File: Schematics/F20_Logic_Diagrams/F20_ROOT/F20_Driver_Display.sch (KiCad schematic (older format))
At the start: 2 parts, among them U5 StepDownConverter, U6 Driver_Display

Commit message: Updated Brakes diagram. Updated power management diagram. Updated relevant library symbols. Updated README.
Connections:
- net labels added: DD_PWR
- net labels removed: PWR_AUX
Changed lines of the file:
@@
 $Descr A 11000 8500
 encoding utf-8
-Sheet 5 6
+Sheet 4 7
 Title "FSAE"
 Date "2020-01-22"
@@
 	2000 3250 2500 3250
 Text GLabel 2000 3000 0    50   Input ~ 0
-PWR_AUX
+DD_PWR
 Wire Wire Line
 	2000 3000 2500 3000

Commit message: Added GND and GND_CHASSIS symbols, updated relevant schematics. Restructured Powertrain hierarchy. Created ECU Connector symbols.
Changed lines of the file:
@@
 $Descr A 11000 8500
 encoding utf-8
-Sheet 4 7
+Sheet 3 7
 Title "FSAE"
-Date "2020-01-22"
-Rev "A"
+Date "2020-02-03"
+Rev "B"
 Comp "F20"
 Comment1 "Alex Domagala"
@@
 	1    0    0    -1
 $EndComp
-$Comp
-L power:GND #PWR?
-U 1 1 5E2A2C36
-P 3500 3500
-F 0 "#PWR?" H 3500 3250 50  0001 C CNN
-F 1 "GND" H 3505 3327 50  0000 C CNN
-F 2 "" H 3500 3500 50  0001 C CNN
-F 3 "" H 3500 3500 50  0001 C CNN
-	1    3500 3500
-	1    0    0    -1
-$EndComp
 Text GLabel 5000 3500 0    50   Input ~ 0
 RIM_DD_RX
@@
 Wire Wire Line
 	5000 4000 8000 4000
-$Comp
-L power:GND #PWR?
-U 1 1 5E29034E
-P 2000 3500
-F 0 "#PWR?" H 2000 3250 50  0001 C CNN
-F 1 "GND" H 2005 3327 50  0000 C CNN
-F 2 "" H 2000 3500 50  0001 C CNN
-F 3 "" H 2000 3500 50  0001 C CNN
-	1    2000 3500
-	1    0    0    -1
-$EndComp
 Wire Wire Line
 	2000 3500 2000 3250
@@
 Wire Wire Line
 	2000 3000 2500 3000
+$Comp
+L FSAE_Library:GND #PWR?
+U 1 1 5E3C0D7F
+P 2000 3500
+F 0 "#PWR?" H 2000 3300 50  0001 C CNN
+F 1 "GND" H 2004 3346 50  0000 C CNN
+F 2 "" H 2000 3450 50  0001 C CNN
+F 3 "" H 2000 3450 50  0001 C CNN
+	1    2000 3500
+	1    0    0    -1
+$EndComp
+$Comp
+L FSAE_Library:GND #PWR?
+U 1 1 5E3C11D7
+P 3500 3500
+F 0 "#PWR?" H 3500 3300 50  0001 C CNN
+F 1 "GND" H 3504 3346 50  0000 C CNN
+F 2 "" H 3500 3450 50  0001 C CNN
+F 3 "" H 3500 3450 50  0001 C CNN
+	1    3500 3500
+	1    0    0    -1
+$EndComp
 $EndSCHEMATC

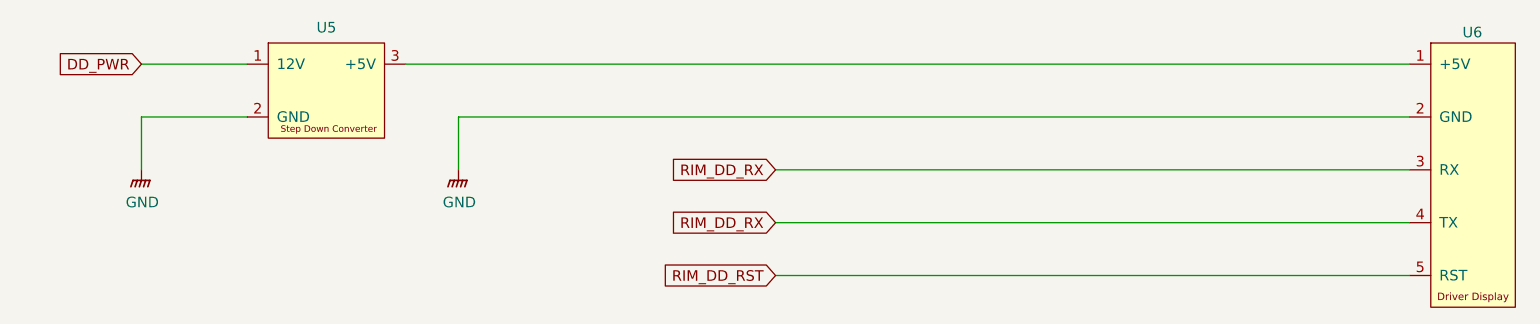
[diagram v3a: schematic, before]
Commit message: Updated per AD commit. O2 sensor schematic, transponder schematic.
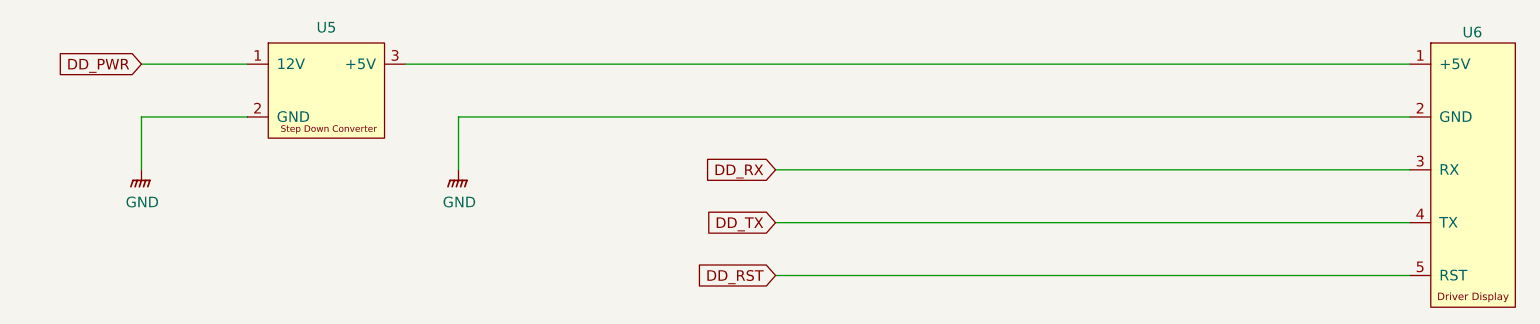
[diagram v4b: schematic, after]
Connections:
- net RIM_DD_RST renamed DD_RST
- net RIM_DD_RX renamed DD_RX
- net DD_RX: no longer U6.4 (TX)
- new net DD_TX: U6.4 (TX)
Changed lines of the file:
@@
 EESchema Schematic File Version 4
-LIBS:F20_ROOT-cache
 EELAYER 30 0
 EELAYER END
 $Descr A 11000 8500
 encoding utf-8
-Sheet 3 7
+Sheet 5 9
 Title "FSAE"
 Date "2020-02-03"
@@
 	1    0    0    -1
 $EndComp
-Text GLabel 5000 3500 0    50   Input ~ 0
-RIM_DD_RX
 Wire Wire Line
 	5000 3500 8000 3500
@@
 Wire Wire Line
 	3500 3250 3500 3500
-Text GLabel 5000 3750 0    50   Input ~ 0
-RIM_DD_RX
 Wire Wire Line
 	5000 3750 8000 3750
 Text GLabel 5000 4000 0    50   Input ~ 0
-RIM_DD_RST
+DD_RST
 Wire Wire Line
 	5000 4000 8000 4000
@@
 	1    0    0    -1
 $EndComp
+Text GLabel 5000 3500 0    50   Input ~ 0
+DD_RX
+Text GLabel 5000 3750 0    50   Input ~ 0
+DD_TX
 $EndSCHEMATC

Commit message: 02/18/20 update
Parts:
- removed U5: StepDownConverter, symbol FSAE_Library:StepDownConverter
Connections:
- net ECU_+5V_1: now reaches U6.1 (+5V)
- net DD_RX renamed RIM_RX3
- net DD_TX renamed RIM_TX3
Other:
- moved on the sheet: U6
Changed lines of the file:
@@
 $Descr A 11000 8500
 encoding utf-8
-Sheet 5 11
+Sheet 7 13
 Title "FSAE"
 Date "2020-02-03"
@@
 L FSAE_Library:Driver_Display U6
 U 1 1 5E291EA2
-P 8000 3000
-F 0 "U6" H 8250 3150 50  0000 L CNN
-F 1 "Driver_Display" H 8300 3150 50  0001 C CNN
-F 2 "" H 8300 3150 50  0001 C CNN
-F 3 "" H 8300 3150 50  0001 C CNN
-	1    8000 3000
-	1    0    0    -1
-$EndComp
-$Comp
-L FSAE_Library:StepDownConverter U5
-U 1 1 5E297DA5
-P 2500 3000
-F 0 "U5" H 2875 3173 50  0000 C CNN
-F 1 "StepDownConverter" H 2750 3150 50  0001 C CNN
-F 2 "" H 3000 3500 50  0001 C CNN
-F 3 "" H 3000 3500 50  0001 C CNN
-	1    2500 3000
+P 7500 3000
+F 0 "U6" H 7750 3150 50  0000 L CNN
+F 1 "Driver_Display" H 7800 3150 50  0001 C CNN
+F 2 "" H 7800 3150 50  0001 C CNN
+F 3 "" H 7800 3150 50  0001 C CNN
+	1    7500 3000
 	1    0    0    -1
 $EndComp
 Wire Wire Line
-	5000 3500 8000 3500
+	4500 3500 7500 3500
 Wire Wire Line
-	3250 3000 8000 3000
+	4500 3000 7500 3000
 Wire Wire Line
-	3500 3250 8000 3250
+	3500 3250 7500 3250
 Wire Wire Line
 	3500 3250 3500 3500
 Wire Wire Line
-	5000 3750 8000 3750
-Text GLabel 5000 4000 0    50   Input ~ 0
+	4500 3750 7500 3750
+Text GLabel 4500 4000 0    50   Input ~ 0
 DD_RST
 Wire Wire Line
-	5000 4000 8000 4000
-Wire Wire Line
-	2000 3500 2000 3250
-Wire Wire Line
-	2000 3250 2500 3250
-Text GLabel 2000 3000 0    50   Input ~ 0
-DD_PWR
-Wire Wire Line
-	2000 3000 2500 3000
+	4500 4000 7500 4000
 $Comp
-L FSAE_Library:GND #PWR0103
-U 1 1 5E3C0D7F
-P 2000 3500
-F 0 "#PWR0103" H 2000 3300 50  0001 C CNN
-F 1 "GND" H 2004 3346 50  0000 C CNN
-F 2 "" H 2000 3450 50  0001 C CNN
-F 3 "" H 2000 3450 50  0001 C CNN
-	1    2000 3500
-	1    0    0    -1
-$EndComp
-$Comp
-L FSAE_Library:GND #PWR0104
+L FSAE_Library:GND #PWR07
 U 1 1 5E3C11D7
 P 3500 3500
-F 0 "#PWR0104" H 3500 3300 50  0001 C CNN
+F 0 "#PWR07" H 3500 3300 50  0001 C CNN
 F 1 "GND" H 3504 3346 50  0000 C CNN
 F 2 "" H 3500 3450 50  0001 C CNN
@@
 	1    0    0    -1
 $EndComp
-Text GLabel 5000 3500 0    50   Input ~ 0
-DD_RX
-Text GLabel 5000 3750 0    50   Input ~ 0
-DD_TX
+Text GLabel 4500 3500 0    50   Input ~ 0
+RIM_RX3
+Text GLabel 4500 3750 0    50   Input ~ 0
+RIM_TX3
+Text GLabel 4500 3000 0    50   Input ~ 0
+ECU_+5V_1
 $EndSCHEMATC

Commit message: 02/19/20 update
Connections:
- net RIM_RX3 renamed DD_RX
- net RIM_TX3 renamed DD_TX
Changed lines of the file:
@@
 	1    0    0    -1
 $EndComp
-Text GLabel 4500 3500 0    50   Input ~ 0
-RIM_RX3
-Text GLabel 4500 3750 0    50   Input ~ 0
-RIM_TX3
+Text GLabel 4500 3500 0    50   BiDi ~ 0
+DD_RX
 Text GLabel 4500 3000 0    50   Input ~ 0
 ECU_+5V_1
+Text GLabel 4500 3750 0    50   BiDi ~ 0
+DD_TX
 $EndSCHEMATC
